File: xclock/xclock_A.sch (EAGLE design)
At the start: 24 parts, among them U1 5P49V5923, X1 9C-24.000MEEJ-T

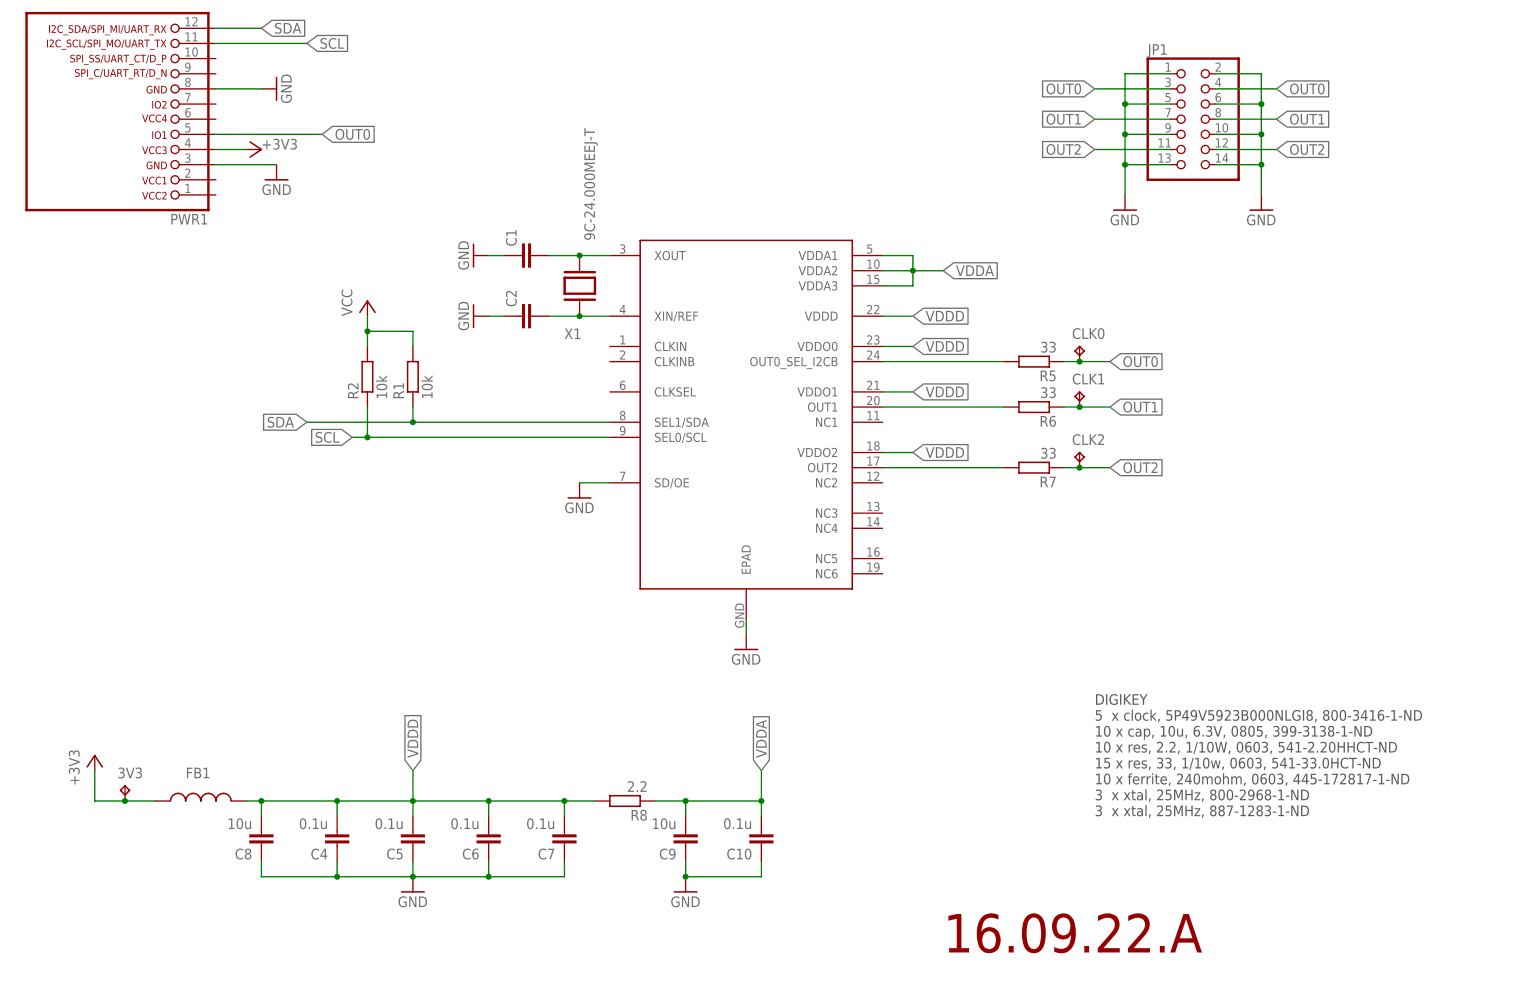
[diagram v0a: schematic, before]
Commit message: xclock: use pinhead 3x7 and added temp sensor.
Signed-off-by: malo <pavol.malosek@gmail.com>
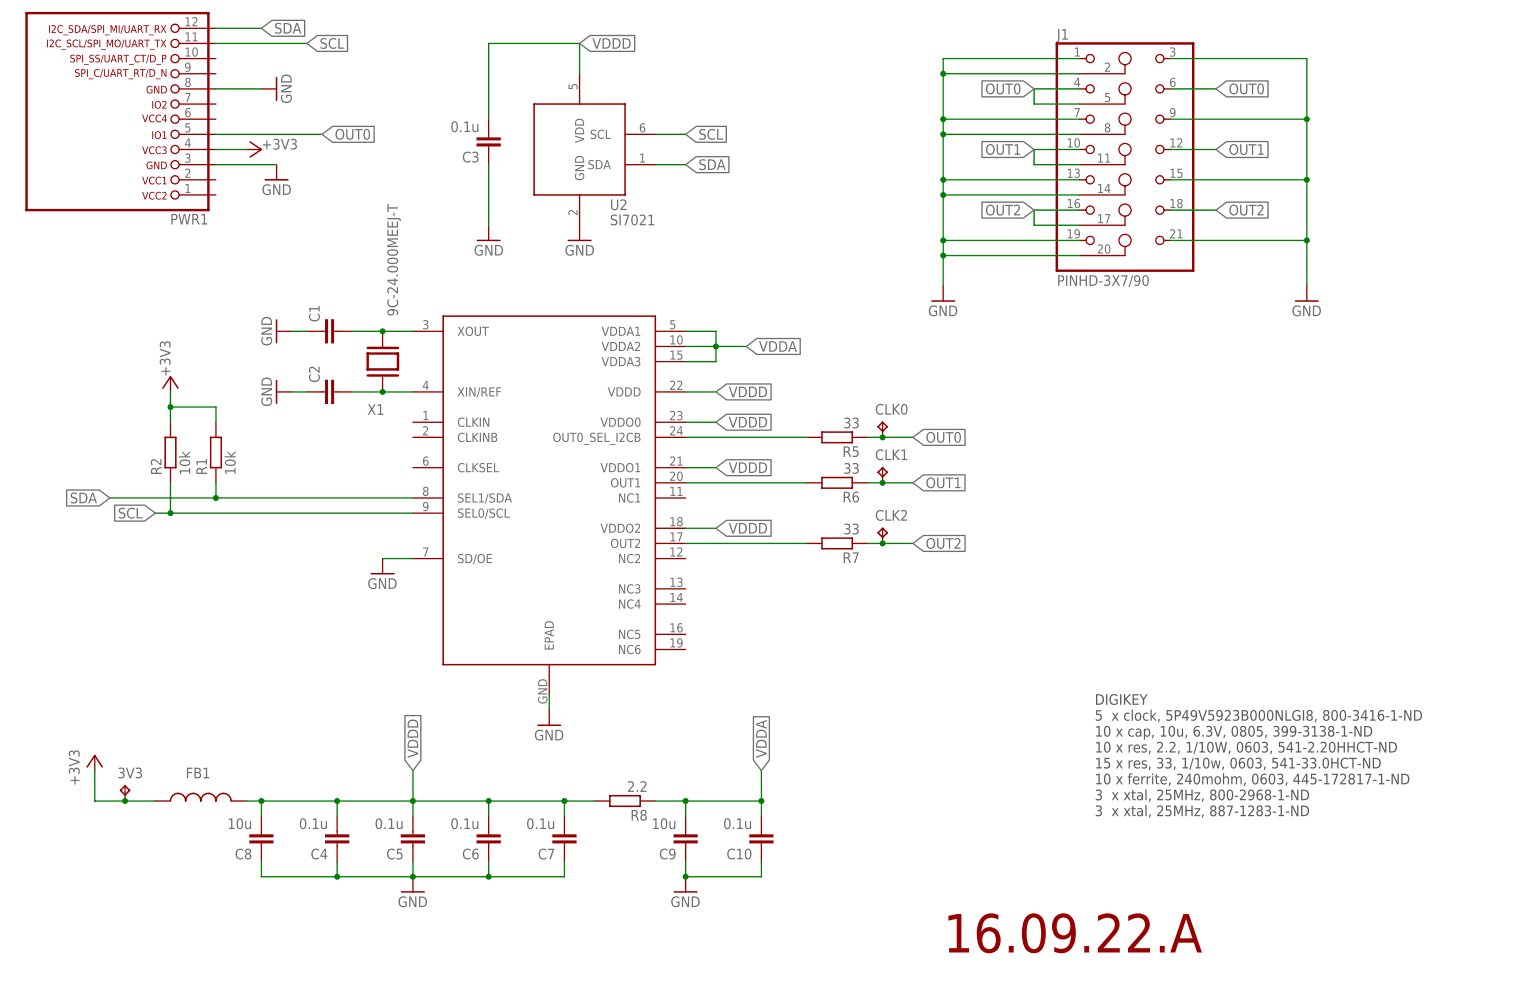
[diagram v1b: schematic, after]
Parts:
- removed JP1: (no value), pinhead:PINHD-2X7/90
- added C3: 0.1u, rcl:C-EUC0603
- added J1: PINHD-3X7/90, pinhead:PINHD-3X7/90
- added U2: SI7021, 25cmsquare:SI7021
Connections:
- net N$1 renamed XOUT
- net N$7 renamed XIN
- removed net VCC: R1.2, R2.2
- net +3V3: now also R1.2, R2.2
- net GND: now also C3.1, J1.1, J1.13, J1.14, J1.15, J1.19, J1.2, J1.20, J1.21, J1.3, J1.7, J1.8, J1.9, U2.GND; no longer JP1.1, JP1.10, JP1.13, JP1.14, JP1.2, JP1.5, JP1.6, JP1.9
- net OUT0: now also J1.4, J1.5, J1.6; no longer JP1.3, JP1.4
- net OUT1: now also J1.10, J1.11, J1.12; no longer JP1.7, JP1.8
- net OUT2: now also J1.16, J1.17, J1.18; no longer JP1.11, JP1.12
- net SCL: now also U2.SCL
- net SDA: now also U2.SDA
- net VDDD: now also C3.2, U2.VDD
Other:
- moved on the sheet: C1, C2, CLK0, CLK1, CLK2, R1, R2, R5, R6, R7, X1

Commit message: xclock: finished + PCB
Signed-off-by: malo <pavol.malosek@gmail.com>
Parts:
- added GND: TEST-22-MULTICOMP, 25cmsquare:TEST-22-MULTICOMP
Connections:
- net GND: now also GND.1
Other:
- note added: "This work is licensed under a Creative Commons Attribution-ShareAlike 4.0 International License. http://creativecommons.org/licenses/by-sa/4.0/"
- note added: "http://25cmsquare.io"
- moved on the sheet: 3V3, C10, C4, C5, C6, C7, C8, C9, FB1, R8

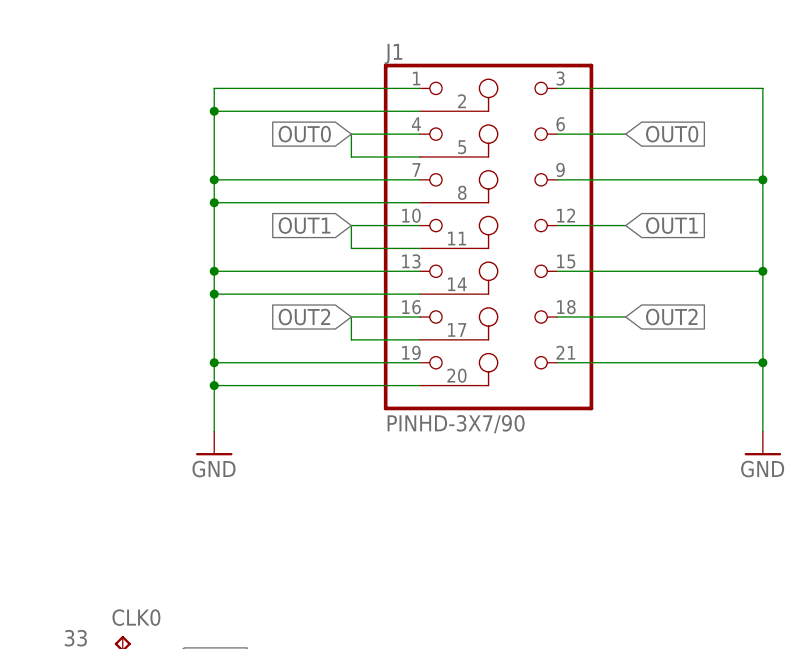
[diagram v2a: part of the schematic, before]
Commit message: xclock: new pinhead 3x7 symbol
Signed-off-by: malo <pavol.malosek@gmail.com>
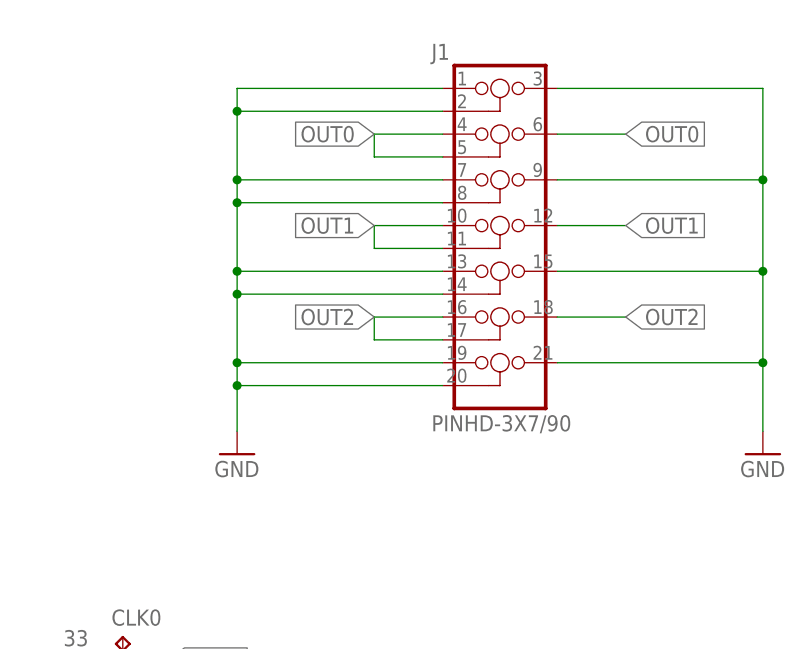
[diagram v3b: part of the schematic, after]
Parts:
- J1: device pinhead:PINHD-3X7/90 -> 25pinhead:PINHD-3X7/90
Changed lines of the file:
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@@
 <part name="+3V7" library="supply1" deviceset="+3V3" device=""/>
 <part name="+3V1" library="supply1" deviceset="+3V3" device=""/>
-<part name="J1" library="pinhead" deviceset="PINHD-3X7" device="/90"/>
 <part name="GND5" library="supply1" deviceset="GND" device=""/>
 <part name="GND6" library="supply1" deviceset="GND" device=""/>
@@
 <part name="GND" library="25cmsquare" deviceset="TEST-22-MULTICOMP" device=""/>
 <part name="GND13" library="supply1" deviceset="GND" device=""/>
+<part name="J1" library="25pinhead" deviceset="PINHD-3X7" device="/90"/>
 </parts>
 <sheets>
@@
 </instance>
 <instance part="+3V1" gate="G$1" x="25.4" y="45.72"/>
-<instance part="J1" gate="G$1" x="200.66" y="147.32"/>
-<instance part="GND5" gate="1" x="167.64" y="119.38"/>
+<instance part="GND5" gate="1" x="170.18" y="119.38"/>
 <instance part="GND6" gate="1" x="228.6" y="119.38"/>
 <instance part="+3V2" gate="G$1" x="38.1" y="106.68" smashed="yes">
@@
 <instance part="GND" gate="G$1" x="22.86" y="22.86" rot="MR90"/>
 <instance part="GND13" gate="1" x="22.86" y="20.32" rot="MR0"/>
+<instance part="J1" gate="G$1" x="200.66" y="144.78"/>
 </instances>
 <busses>
@@
 </segment>
 <segment>
+<wire x1="193.04" y1="160.02" x2="170.18" y2="160.02" width="0.1524" layer="91"/>
+<wire x1="170.18" y1="160.02" x2="170.18" y2="157.48" width="0.1524" layer="91"/>
+<wire x1="170.18" y1="157.48" x2="170.18" y2="149.86" width="0.1524" layer="91"/>
+<wire x1="170.18" y1="149.86" x2="170.18" y2="147.32" width="0.1524" layer="91"/>
+<wire x1="170.18" y1="147.32" x2="170.18" y2="139.7" width="0.1524" layer="91"/>
+<wire x1="170.18" y1="139.7" x2="170.18" y2="137.16" width="0.1524" layer="91"/>
+<wire x1="170.18" y1="137.16" x2="170.18" y2="129.54" width="0.1524" layer="91"/>
+<wire x1="170.18" y1="129.54" x2="170.18" y2="127" width="0.1524" layer="91"/>
+<wire x1="170.18" y1="127" x2="170.18" y2="121.92" width="0.1524" layer="91"/>
+<wire x1="193.04" y1="149.86" x2="170.18" y2="149.86" width="0.1524" layer="91"/>
+<junction x="170.18" y="149.86"/>
+<wire x1="193.04" y1="139.7" x2="170.18" y2="139.7" width="0.1524" layer="91"/>
+<junction x="170.18" y="139.7"/>
+<wire x1="193.04" y1="129.54" x2="170.18" y2="129.54" width="0.1524" layer="91"/>
+<junction x="170.18" y="129.54"/>
+<wire x1="193.04" y1="157.48" x2="170.18" y2="157.48" width="0.1524" layer="91"/>
+<junction x="170.18" y="157.48"/>
+<wire x1="193.04" y1="147.32" x2="170.18" y2="147.32" width="0.1524" layer="91"/>
+<junction x="170.18" y="147.32"/>
+<wire x1="193.04" y1="137.16" x2="170.18" y2="137.16" width="0.1524" layer="91"/>
+<junction x="170.18" y="137.16"/>
+<wire x1="193.04" y1="127" x2="170.18" y2="127" width="0.1524" layer="91"/>
+<junction x="170.18" y="127"/>
+<pinref part="GND5" gate="1" pin="GND"/>
 <pinref part="J1" gate="G$1" pin="1"/>
-<wire x1="190.5" y1="160.02" x2="167.64" y2="160.02" width="0.1524" layer="91"/>
-<wire x1="167.64" y1="160.02" x2="167.64" y2="157.48" width="0.1524" layer="91"/>
+<pinref part="J1" gate="G$1" pin="2"/>
 <pinref part="J1" gate="G$1" pin="7"/>
-<wire x1="167.64" y1="157.48" x2="167.64" y2="149.86" width="0.1524" layer="91"/>
-<wire x1="167.64" y1="149.86" x2="167.64" y2="147.32" width="0.1524" layer="91"/>
-<wire x1="167.64" y1="147.32" x2="167.64" y2="139.7" width="0.1524" layer="91"/>
-<wire x1="167.64" y1="139.7" x2="167.64" y2="137.16" width="0.1524" layer="91"/>
-<wire x1="167.64" y1="137.16" x2="167.64" y2="129.54" width="0.1524" layer="91"/>
-<wire x1="167.64" y1="129.54" x2="167.64" y2="127" width="0.1524" layer="91"/>
-<wire x1="167.64" y1="127" x2="167.64" y2="121.92" width="0.1524" layer="91"/>
-<wire x1="190.5" y1="149.86" x2="167.64" y2="149.86" width="0.1524" layer="91"/>
-<junction x="167.64" y="149.86"/>
+<pinref part="J1" gate="G$1" pin="8"/>
 <pinref part="J1" gate="G$1" pin="13"/>
-<wire x1="190.5" y1="139.7" x2="167.64" y2="139.7" width="0.1524" layer="91"/>
-<junction x="167.64" y="139.7"/>
+<pinref part="J1" gate="G$1" pin="14"/>
 <pinref part="J1" gate="G$1" pin="19"/>
-<wire x1="190.5" y1="129.54" x2="167.64" y2="129.54" width="0.1524" layer="91"/>
-<junction x="167.64" y="129.54"/>
-<pinref part="J1" gate="G$1" pin="2"/>
-<wire x1="190.5" y1="157.48" x2="167.64" y2="157.48" width="0.1524" layer="91"/>
-<junction x="167.64" y="157.48"/>
-<pinref part="J1" gate="G$1" pin="8"/>
-<wire x1="190.5" y1="147.32" x2="167.64" y2="147.32" width="0.1524" layer="91"/>
-<junction x="167.64" y="147.32"/>
-<pinref part="J1" gate="G$1" pin="14"/>
-<wire x1="190.5" y1="137.16" x2="167.64" y2="137.16" width="0.1524" layer="91"/>
-<junction x="167.64" y="137.16"/>
 <pinref part="J1" gate="G$1" pin="20"/>
-<wire x1="190.5" y1="127" x2="167.64" y2="127" width="0.1524" layer="91"/>
-<junction x="167.64" y="127"/>
-<pinref part="GND5" gate="1" pin="GND"/>
-</segment>
-<segment>
-<pinref part="J1" gate="G$1" pin="3"/>
+</segment>
+<segment>
 <wire x1="205.74" y1="160.02" x2="228.6" y2="160.02" width="0.1524" layer="91"/>
 <wire x1="228.6" y1="160.02" x2="228.6" y2="149.86" width="0.1524" layer="91"/>
-<pinref part="J1" gate="G$1" pin="21"/>
 <wire x1="228.6" y1="149.86" x2="228.6" y2="139.7" width="0.1524" layer="91"/>
 <wire x1="228.6" y1="139.7" x2="228.6" y2="129.54" width="0.1524" layer="91"/>
@@
 <wire x1="205.74" y1="129.54" x2="228.6" y2="129.54" width="0.1524" layer="91"/>
 <junction x="228.6" y="129.54"/>
-<pinref part="J1" gate="G$1" pin="15"/>
 <wire x1="205.74" y1="139.7" x2="228.6" y2="139.7" width="0.1524" layer="91"/>
 <junction x="228.6" y="139.7"/>
-<pinref part="J1" gate="G$1" pin="9"/>
 <wire x1="205.74" y1="149.86" x2="228.6" y2="149.86" width="0.1524" layer="91"/>
 <junction x="228.6" y="149.86"/>
 <pinref part="GND6" gate="1" pin="GND"/>
+<pinref part="J1" gate="G$1" pin="3"/>
+<pinref part="J1" gate="G$1" pin="9"/>
+<pinref part="J1" gate="G$1" pin="15"/>
+<pinref part="J1" gate="G$1" pin="21"/>
 </segment>
 <segment>
@@
 </segment>
 <segment>
+<wire x1="193.04" y1="154.94" x2="185.42" y2="154.94" width="0.1524" layer="91"/>
+<wire x1="185.42" y1="154.94" x2="185.42" y2="152.4" width="0.1524" layer="91"/>
+<wire x1="185.42" y1="152.4" x2="193.04" y2="152.4" width="0.1524" layer="91"/>
+<label x="185.42" y="154.94" size="1.778" layer="95" rot="R180" xref="yes"/>
 <pinref part="J1" gate="G$1" pin="4"/>
-<wire x1="190.5" y1="154.94" x2="182.88" y2="154.94" width="0.1524" layer="91"/>
-<wire x1="182.88" y1="154.94" x2="182.88" y2="152.4" width="0.1524" layer="91"/>
 <pinref part="J1" gate="G$1" pin="5"/>
-<wire x1="182.88" y1="152.4" x2="190.5" y2="152.4" width="0.1524" layer="91"/>
-<label x="182.88" y="154.94" size="1.778" layer="95" rot="R180" xref="yes"/>
-</segment>
-<segment>
-<pinref part="J1" gate="G$1" pin="6"/>
+</segment>
+<segment>
 <wire x1="205.74" y1="154.94" x2="213.36" y2="154.94" width="0.1524" layer="91"/>
 <label x="213.36" y="154.94" size="1.778" layer="95" xref="yes"/>
+<pinref part="J1" gate="G$1" pin="6"/>
 </segment>
 </net>
@@
 </segment>
 <segment>
+<wire x1="193.04" y1="144.78" x2="185.42" y2="144.78" width="0.1524" layer="91"/>
+<wire x1="185.42" y1="144.78" x2="185.42" y2="142.24" width="0.1524" layer="91"/>
+<wire x1="185.42" y1="142.24" x2="193.04" y2="142.24" width="0.1524" layer="91"/>
+<label x="185.42" y="144.78" size="1.778" layer="95" rot="R180" xref="yes"/>
 <pinref part="J1" gate="G$1" pin="10"/>
-<wire x1="190.5" y1="144.78" x2="182.88" y2="144.78" width="0.1524" layer="91"/>
-<wire x1="182.88" y1="144.78" x2="182.88" y2="142.24" width="0.1524" layer="91"/>
 <pinref part="J1" gate="G$1" pin="11"/>
-<wire x1="182.88" y1="142.24" x2="190.5" y2="142.24" width="0.1524" layer="91"/>
-<label x="182.88" y="144.78" size="1.778" layer="95" rot="R180" xref="yes"/>
-</segment>
-<segment>
-<pinref part="J1" gate="G$1" pin="12"/>
+</segment>
+<segment>
 <wire x1="205.74" y1="144.78" x2="213.36" y2="144.78" width="0.1524" layer="91"/>
 <label x="213.36" y="144.78" size="1.778" layer="95" xref="yes"/>
+<pinref part="J1" gate="G$1" pin="12"/>
 </segment>
 </net>
@@
 </segment>
 <segment>
+<wire x1="193.04" y1="134.62" x2="185.42" y2="134.62" width="0.1524" layer="91"/>
+<wire x1="185.42" y1="134.62" x2="185.42" y2="132.08" width="0.1524" layer="91"/>
+<wire x1="185.42" y1="132.08" x2="193.04" y2="132.08" width="0.1524" layer="91"/>
+<label x="185.42" y="134.62" size="1.778" layer="95" rot="R180" xref="yes"/>
 <pinref part="J1" gate="G$1" pin="16"/>
-<wire x1="190.5" y1="134.62" x2="182.88" y2="134.62" width="0.1524" layer="91"/>
-<wire x1="182.88" y1="134.62" x2="182.88" y2="132.08" width="0.1524" layer="91"/>
 <pinref part="J1" gate="G$1" pin="17"/>
-<wire x1="182.88" y1="132.08" x2="190.5" y2="132.08" width="0.1524" layer="91"/>
-<label x="182.88" y="134.62" size="1.778" layer="95" rot="R180" xref="yes"/>
-</segment>
-<segment>
-<pinref part="J1" gate="G$1" pin="18"/>
+</segment>
+<segment>
 <wire x1="205.74" y1="134.62" x2="213.36" y2="134.62" width="0.1524" layer="91"/>
 <label x="213.36" y="134.62" size="1.778" layer="95" xref="yes"/>
-</segment>
-</net>
+<pinref part="J1" gate="G$1" pin="18"/>
+</segment>
+</net>
